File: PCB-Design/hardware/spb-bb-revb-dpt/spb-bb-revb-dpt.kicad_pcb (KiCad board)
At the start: 4 copper layers, 89.5 x 85.2 mm, 195 parts, among them J1 DC+, J10 U.FL L2, J11 U.FL D2, J12 V_ISO,HS in: 1 +, 2 -, J13 V_ISO,LS in: 1 +, 2 -, J14 CTRL2: 1 RTN 2 PWMH 3 RTN 4 P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, J15 U.FL H3, J16 U.FL L3, J17 U.FL D3, J18 U.FL H4, J19 U.FL L4, J2 DC-, J20 U.FL D4, J21 AC, J3 V_ISO,HS in: 1 +, 2 -, J4 V_ISO,LS in: 1 +, 2 -, J5 CTRL1: 1 RTN 2 PWMH 3 RTN 4 P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, J6 U.FL H1, J7 U.FL L1, J8 U.FL D1, J9 U.FL H2, Q1 EPC2361, Q2 EPC2361, Q3 EPC2361, Q4 EPC2361, Q5 EPC2361, Q6 EPC2361, Q7 EPC2361, Q8 EPC2361, U1 2EDF7275K, U2 2EDF7275K

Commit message: Rev B boards: driver output-side 1 uF bypass to 25 V (TDK C1608X7R1E105K080AB)
C13-C16 / C46-C49 (VDD-Kelvin and Kelvin-VEE of each driver output, at most
5.1 V and ~4 V): the 16 V Murata GRM188R71C105KA12D is end of life. Same 0603
footprint, 25 V X7R keeps more of its 1 uF under the DC bias. DRC 0/0 and
schematic = PCB on both boards; fab outputs rebuilt.

Co-Authored-By: Claude Opus 5.5 <noreply@anthropic.com>
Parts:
- C13, C14, C15, C16, C46, C47, C48, C49: value 1uF 16V X7R 0603 -> 1uF 25V X7R 0603

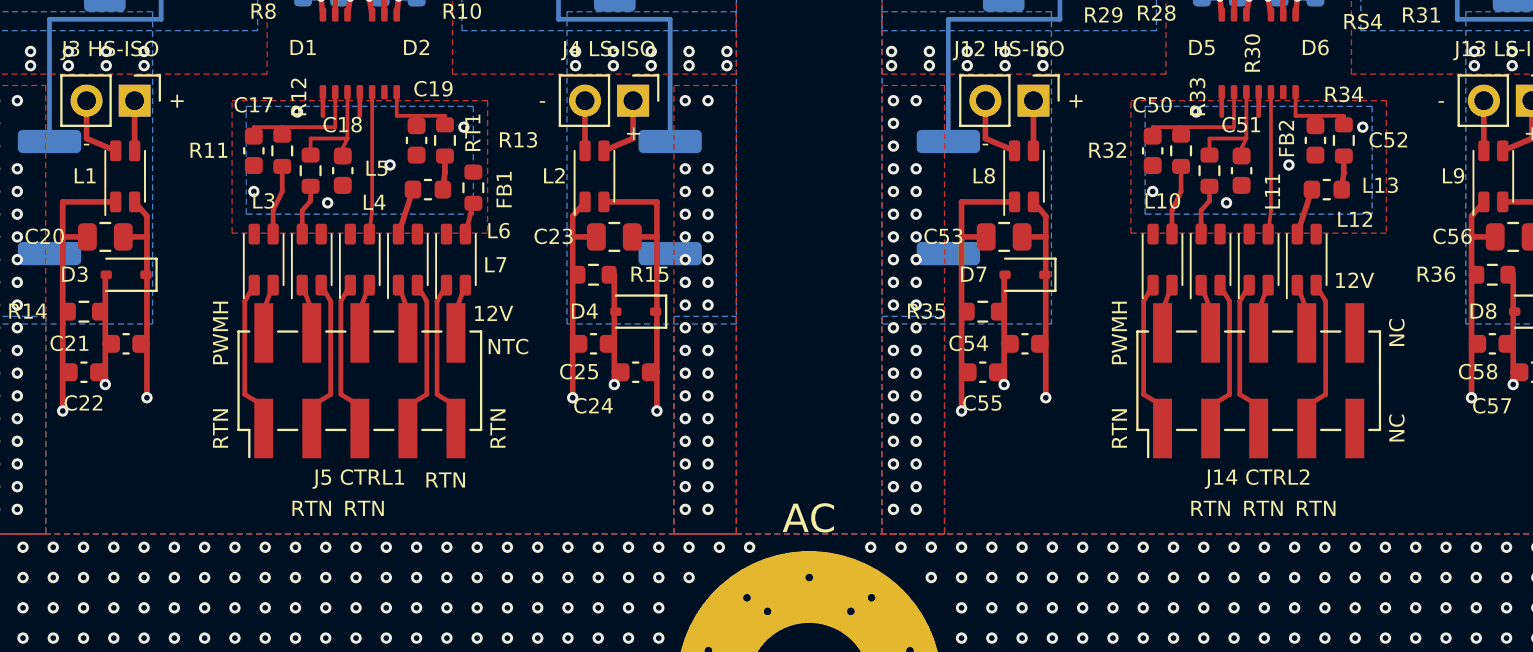
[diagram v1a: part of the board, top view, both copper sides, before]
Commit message: Rev B boards: control-header silk legend
The 2x5 control header (J5 CTRL1, J14 CTRL2) had labels only on its outer
pins and the connector name centred under it, where it read like a pin label.
Now each signal name is printed vertically under its own column, the rows are
marked SIG (choke side) and RTN, and the connector name sits beside the
header. DRC 0/0 and schematic = PCB on both boards; fab outputs and renders
rebuilt.

Co-Authored-By: Claude Opus 5.5 <noreply@anthropic.com>
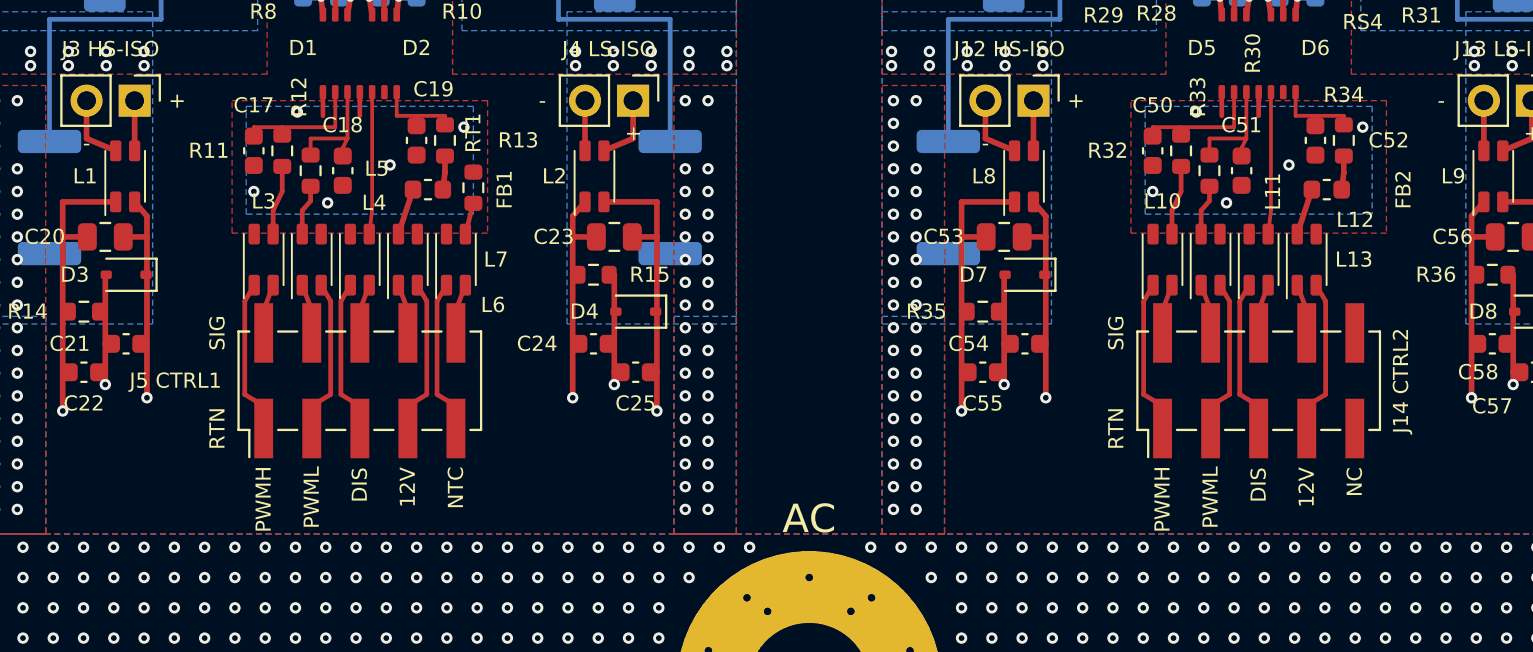
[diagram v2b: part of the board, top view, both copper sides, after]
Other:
- board text added: "DIS"
- board text added: "PWML"
- board text added: "SIG"

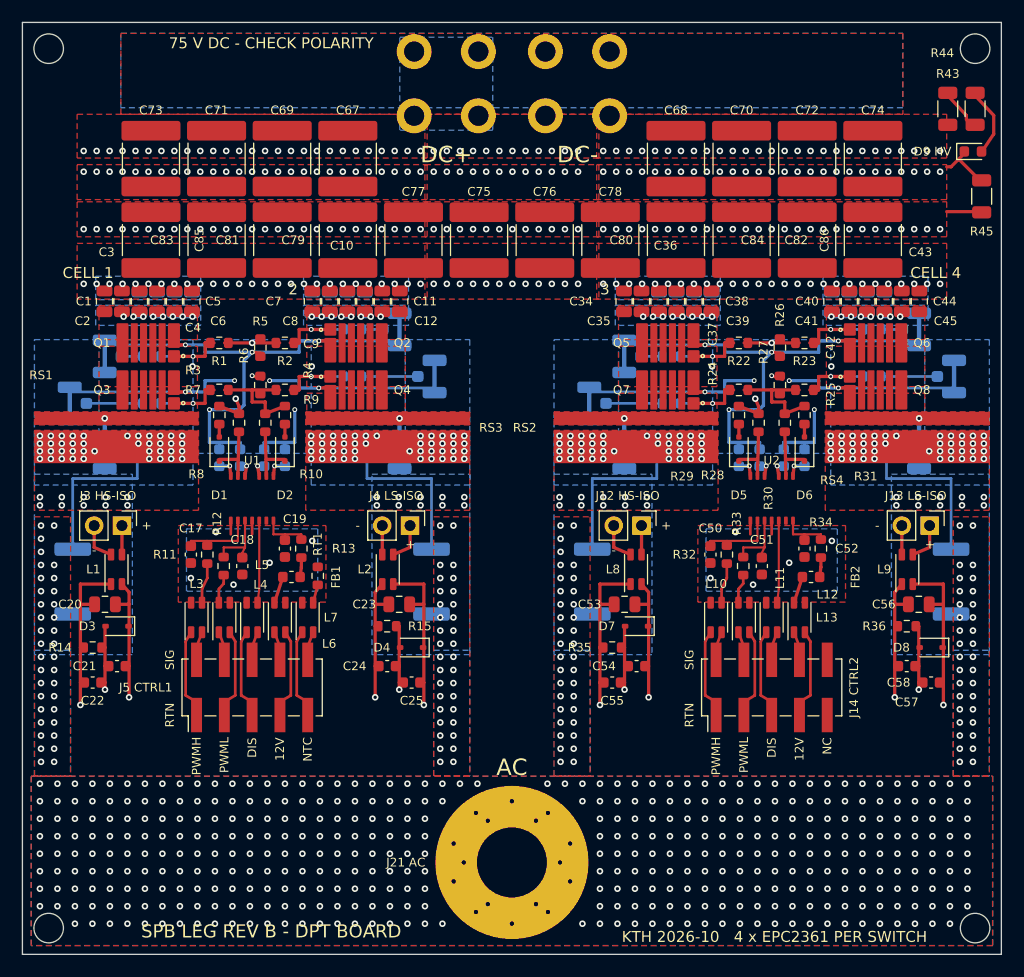
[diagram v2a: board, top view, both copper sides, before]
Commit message: Rev B boards: V_DS U.FL directly on the switch node; pad map regenerated with the board
- V_DS LS ports: the 4.99 k 2512 divider is removed (its 50 R side ran
  ~15 mm over switch-node copper, ~2 pF -> volts of injected error). The
  centre pin sits on the switch node, shield on LSRC; DPT only, 1 MOhm scope
  input, never 50 R. U.FL-R-SMT-1(01) (100 V listed) for these ports.
  The connector's own pin-to-shield gap is excepted from the 0.5 mm rule;
  bottom silk: "VDS U.FL = 75 V: 1 MOHM SCOPE INPUT ONLY".
- The generator now writes pad_nets.json itself. It had not been refreshed
  since 2026-10-16 13:53, so the schematics and the schematic check of the
  later commits ran on a stale pad map; both boards now check against the
  real board data: 0 problems.

Co-Authored-By: Claude Opus 5.5 <noreply@anthropic.com>
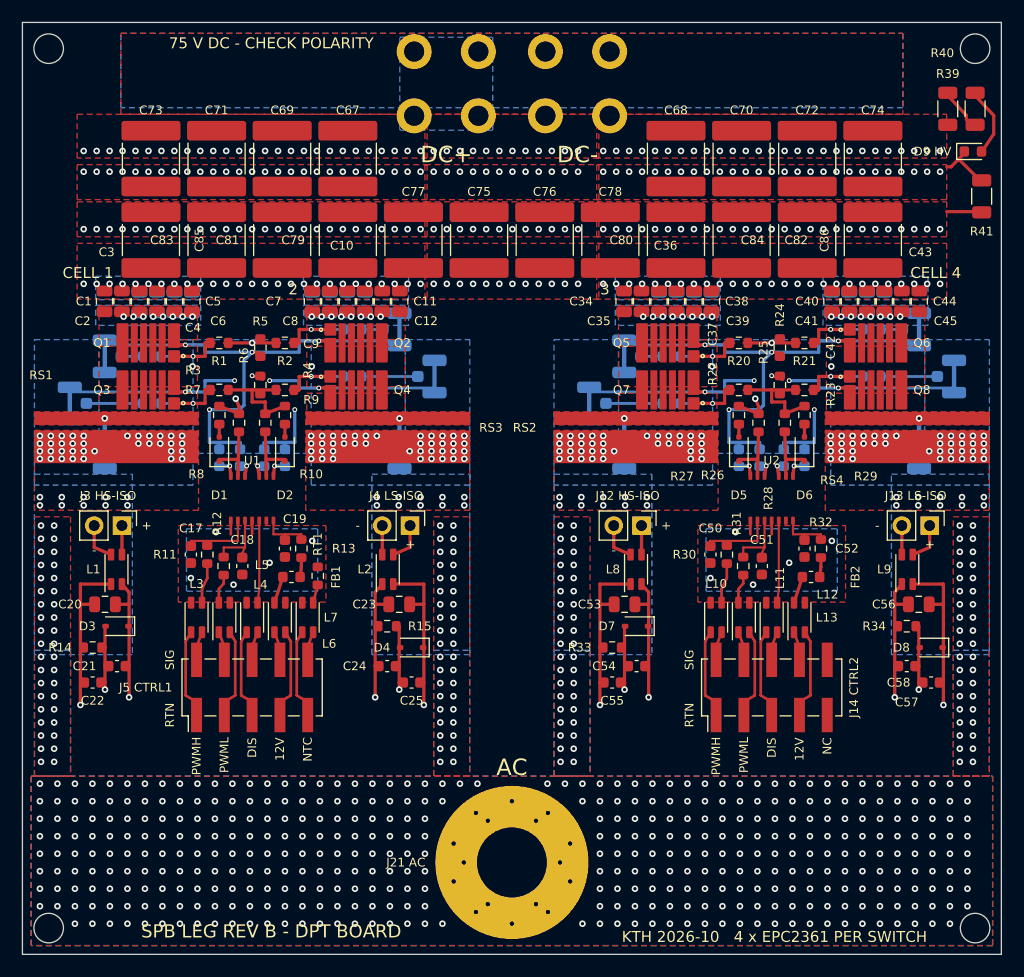
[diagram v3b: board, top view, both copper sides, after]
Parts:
- removed R42: 4.99k 1% 2512 (V_DS LS, 100:1 into 50 R), Resistor_SMD:R_2512_6332Metric
- removed R43, R44: 68k 1206 (HV LED), Resistor_SMD:R_1206_3216Metric
- removed R45: 100k 1206 (bleeder), Resistor_SMD:R_1206_3216Metric
- R18: value 4.99k 1% 2512 (V_DS LS, 100:1 into 50 R) -> 0R (V_GS HS); footprint Resistor_SMD:R_2512_6332Metric -> Resistor_SMD:R_0603_1608Metric
- R19: value 0R (V_GS HS) -> 0R (V_GS LS)
- R20: value 0R (V_GS LS) -> 0R5 1% (R_G HL); moved to F.Cu
- R21: value 4.99k 1% 2512 (V_DS LS, 100:1 into 50 R) -> 0R5 1% (R_G HR); footprint Resistor_SMD:R_2512_6332Metric -> Resistor_SMD:R_0603_1608Metric; moved to F.Cu
- R22: value 0R5 1% (R_G HL) -> 0R5 1% (R_G LL)
- R23: value 0R5 1% (R_G HR) -> 0R5 1% (R_G LR)
- R24: value 0R5 1% (R_G LL) -> 10k 1% (HS gate pull-down)
- R25: value 0R5 1% (R_G LR) -> 10k 1% (LS gate pull-down)
- R26: value 10k 1% (HS gate pull-down) -> 0R75 1% (R_ON,A)
- R27: value 10k 1% (LS gate pull-down) -> 0R (R_OFF,A)
- R28: value 0R75 1% (R_ON,A) -> 0R75 1% (R_ON,B)
- R29: value 0R (R_OFF,A) -> 0R (R_OFF,B)
- R30: value 0R75 1% (R_ON,B) -> 47R 1% (INA)
- R31: value 0R (R_OFF,B) -> 47R 1% (INB)
- R32: value 47R 1% (INA) -> 3k 1% (RVDDI)
- R33: value 47R 1% (INB) -> 150R 1% 0603 (bias, <= 82 mW)
- R34: value 3k 1% (RVDDI) -> 150R 1% 0603 (bias, <= 82 mW)
- R35: value 150R 1% 0603 (bias, <= 82 mW) -> 0R (V_GS HS); moved to B.Cu
- R36: value 150R 1% 0603 (bias, <= 82 mW) -> 0R (V_GS LS); moved to B.Cu
- R39: value 4.99k 1% 2512 (V_DS LS, 100:1 into 50 R) -> 68k 1206 (HV LED); footprint Resistor_SMD:R_2512_6332Metric -> Resistor_SMD:R_1206_3216Metric; moved to F.Cu
- R40: value 0R (V_GS HS) -> 68k 1206 (HV LED); footprint Resistor_SMD:R_0603_1608Metric -> Resistor_SMD:R_1206_3216Metric; moved to F.Cu
- R41: value 0R (V_GS LS) -> 100k 1206 (bleeder); footprint Resistor_SMD:R_0603_1608Metric -> Resistor_SMD:R_1206_3216Metric; moved to F.Cu
- moved R39 54.1 mm to (189.8, 83.5), turned to 90 degrees
- moved R21 40.5 mm to (176.8, 104.9), turned to 0 degrees
- moved R20 35.4 mm to (170.8, 104.9)
- moved R18 34.4 mm to (135.4, 103.7), turned to 0 degrees
- moved R36 29.7 mm to (164.6, 110.4)
- moved R35 27.2 mm to (164.6, 106.1)
- moved R40 22.3 mm to (192.3, 83.5), turned to 90 degrees
- moved R41 19.3 mm to (192.9, 91.5), turned to 90 degrees
- moved R38 18.6 mm to (182.9, 108.0)
- moved R37 18.6 mm to (182.9, 103.7)
- moved R31 14.9 mm to (171.2, 125.3)
- moved R33 14.1 mm to (159.2, 132.8), turned to 0 degrees
- moved R30 13.2 mm to (169.7, 124.2)
- moved R34 10.6 mm to (186.1, 130.8), turned to 0 degrees
- moved R32 8.62 mm to (178.2, 123.7)
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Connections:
- J11 pad 1: UFL_D2 -> SW
- J17 pad 1: UFL_D3 -> SW
- J20 pad 1: UFL_D4 -> SW
- J8 pad 1: UFL_D1 -> SW
- R18 pad 1: UFL_D1 -> GH_R1
- R18 pad 2: SW -> UFL_H2
- R19 pad 1: GH_R1 -> GL_R1
- R19 pad 2: UFL_H2 -> UFL_L2
- R20 pad 1: GL_R1 -> GH_L2
- R20 pad 2: UFL_L2 -> GH_STAR2
- R21 pad 1: UFL_D2 -> GH_STAR2
- R21 pad 2: SW -> GH_R2
- R22 pad 1: GH_L2 -> GL_L2
- R22 pad 2: GH_STAR2 -> GL_STAR2
- R23 pad 1: GH_STAR2 -> GL_STAR2
- R23 pad 2: GH_R2 -> GL_R2
- R24 pad 1: GL_L2 -> KH2
- R24 pad 2: GL_STAR2 -> GH_STAR2
- R25 pad 2: GL_R2 -> KL2
- R26 pad 1: KH2 -> OUTA2
- R27 pad 1: GL_STAR2 -> OFFA2
- R27 pad 2: KL2 -> GH_STAR2
- R28 pad 1: OUTA2 -> OUTB2
- R28 pad 2: GH_STAR2 -> GL_STAR2
- R29 pad 1: OFFA2 -> OFFB2
- R29 pad 2: GH_STAR2 -> GL_STAR2
- R30 pad 1: OUTB2 -> PWM_H2
- R30 pad 2: GL_STAR2 -> INA2
- R31 pad 1: OFFB2 -> PWM_L2
- R31 pad 2: GL_STAR2 -> INB2
- R32 pad 1: PWM_H2 -> +12V2
- R32 pad 2: INA2 -> VDDI2
- R33 pad 1: PWM_L2 -> VEEA2
- R33 pad 2: INB2 -> KH2
- R34 pad 1: +12V2 -> VEEB2
- R34 pad 2: VDDI2 -> KL2
- R35 pad 1: VEEA2 -> UFL_H3
- R35 pad 2: KH2 -> GH_L2
- R36 pad 1: VEEB2 -> UFL_L3
- R36 pad 2: KL2 -> GL_L2
- R37 pad 1: UFL_H3 -> GH_R2
- R37 pad 2: GH_L2 -> UFL_H4
- R38 pad 1: UFL_L3 -> GL_R2
- R38 pad 2: GL_L2 -> UFL_L4
- R39 pad 1: UFL_D3 -> DCP
- R39 pad 2: SW -> HVA
- R40 pad 1: GH_R2 -> HVA
- R40 pad 2: UFL_H4 -> HVB
- R41 pad 1: GL_R2 -> DCP
- R41 pad 2: UFL_L4 -> DCN
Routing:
- net UFL_D1: track 16.2 -> 0.00 mm
- net UFL_D4: track 16.2 -> 0.00 mm
- net UFL_D3: track 16.2 -> 0.00 mm
- net UFL_D2: track 16.2 -> 0.00 mm
- net SW: track 0.00 -> 14.3 mm, vias 556 -> 568
- net DCN: vias 340 -> 324
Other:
- board text added: "VDS U.FL = 75 V: 1 MOHM SCOPE INPUT ONLY"
- board text removed: "R42"
- board text removed: "R43"
- board text removed: "R44"
- board text removed: "R45"
